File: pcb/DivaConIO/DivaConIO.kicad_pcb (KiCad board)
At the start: 2 copper layers, 70 x 75 mm, 67 parts, among them J1 B6B-PH-SM4-TBT, J2 B4B-PH-SM4-TBT, J3 B6B-PH-SM4-TBT, J4 B5B-PH-SM4-TBT, J5 B8B-PH-SM4-TBT, J6 B6B-PH-SM4-TBT, J7 BM03B-SRSS-TBT, SW1 SKRPABE010, U1 74HCT1G14GV,125, U2 ULN2003D1013TR

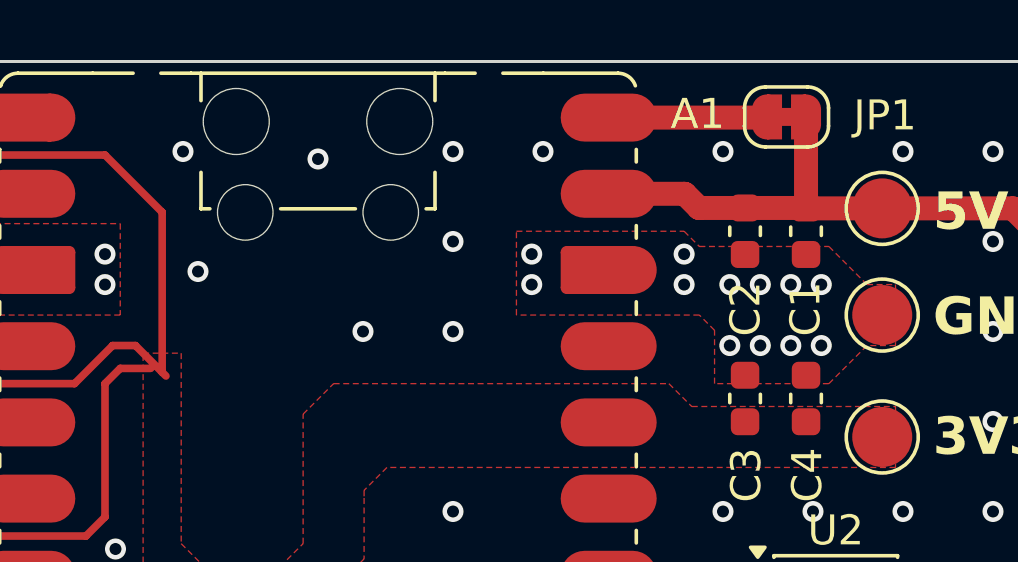
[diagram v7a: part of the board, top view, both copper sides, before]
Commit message: Generate slider PCB 3d model
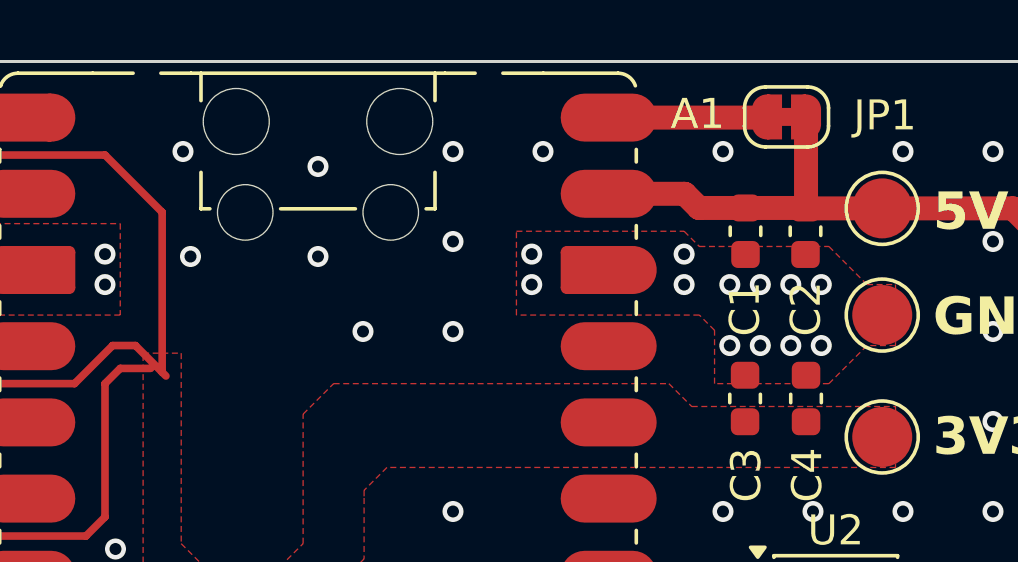
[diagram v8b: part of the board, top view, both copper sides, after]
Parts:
- moved C1 2.02 mm to (156.8, 50.7)
- moved C2 2.01 mm to (158.8, 50.7)
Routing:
- net GND: vias 439 -> 440
